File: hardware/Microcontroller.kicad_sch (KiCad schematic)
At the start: 93 parts, among them J10 UART, J2 USB_C, J3 OLED, J8 +12V, J9 STLink, Q4 IRLML2244, Q5 MMBT3904, SW1 Button Up, SW2 Button Down, SW3 Reset, SW4 Button Escape, SW5 Button Left, SW6 Button Enter, SW7 Button Right, SW8 Button Power, U10 STM32F405RGTx, U11 TPS7A2033, U2 TP6841S6, U3 USBLC6-2, Y1 8 MHz

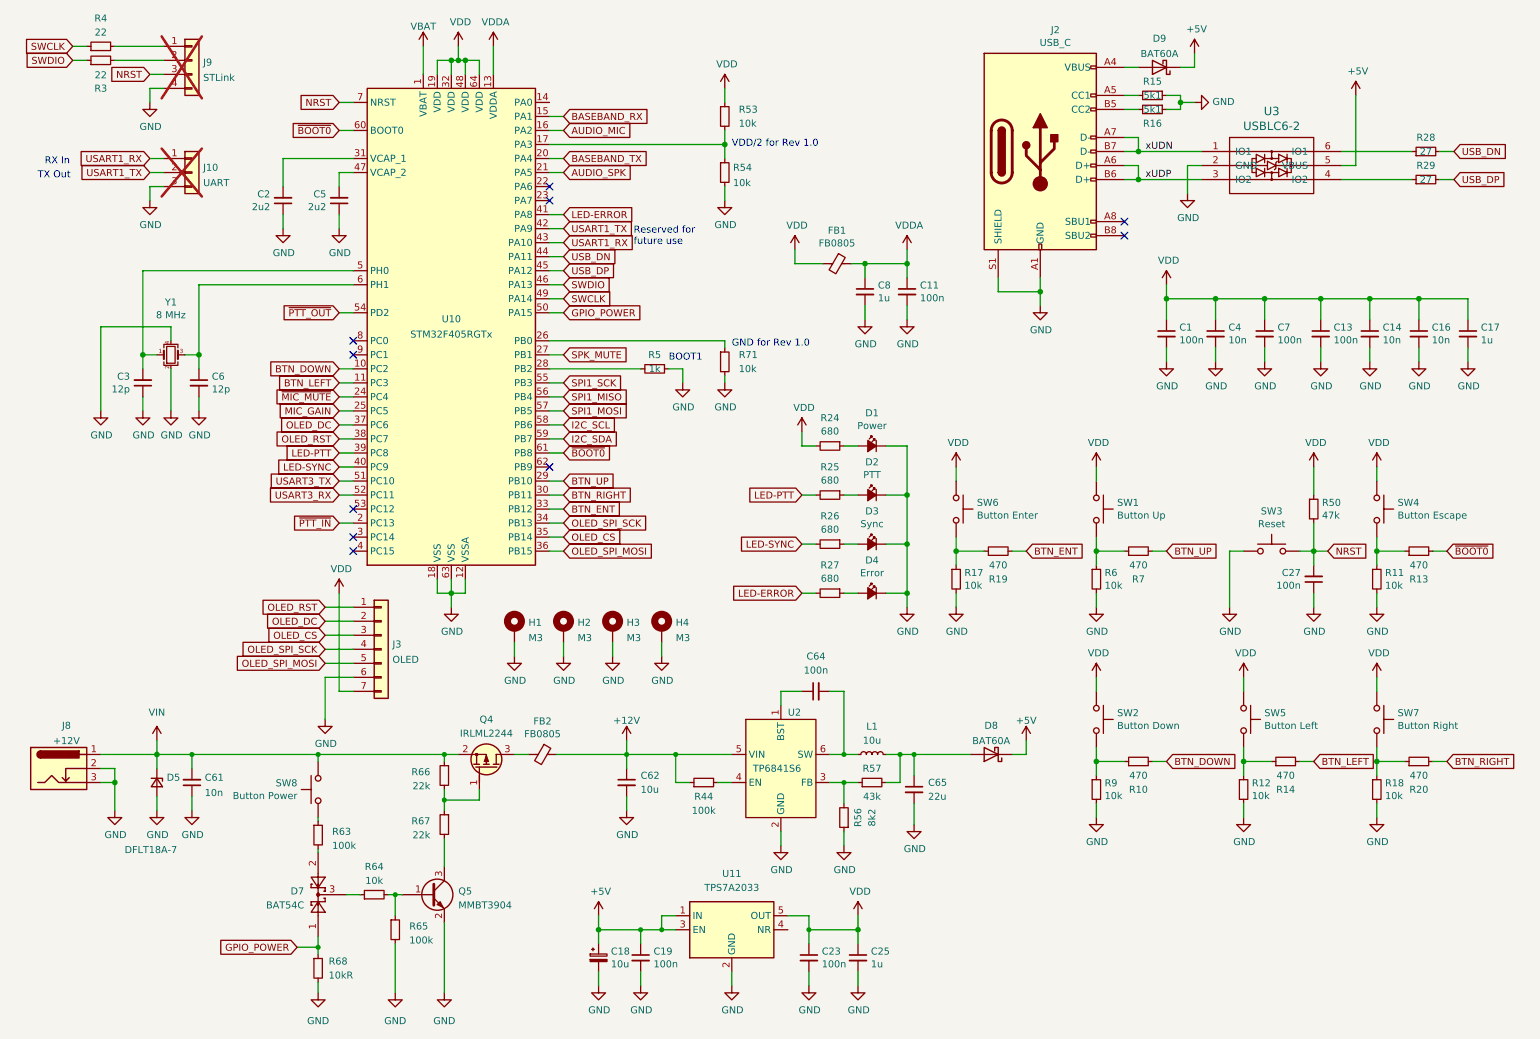
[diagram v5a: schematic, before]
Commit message: Reworked audio output diagram
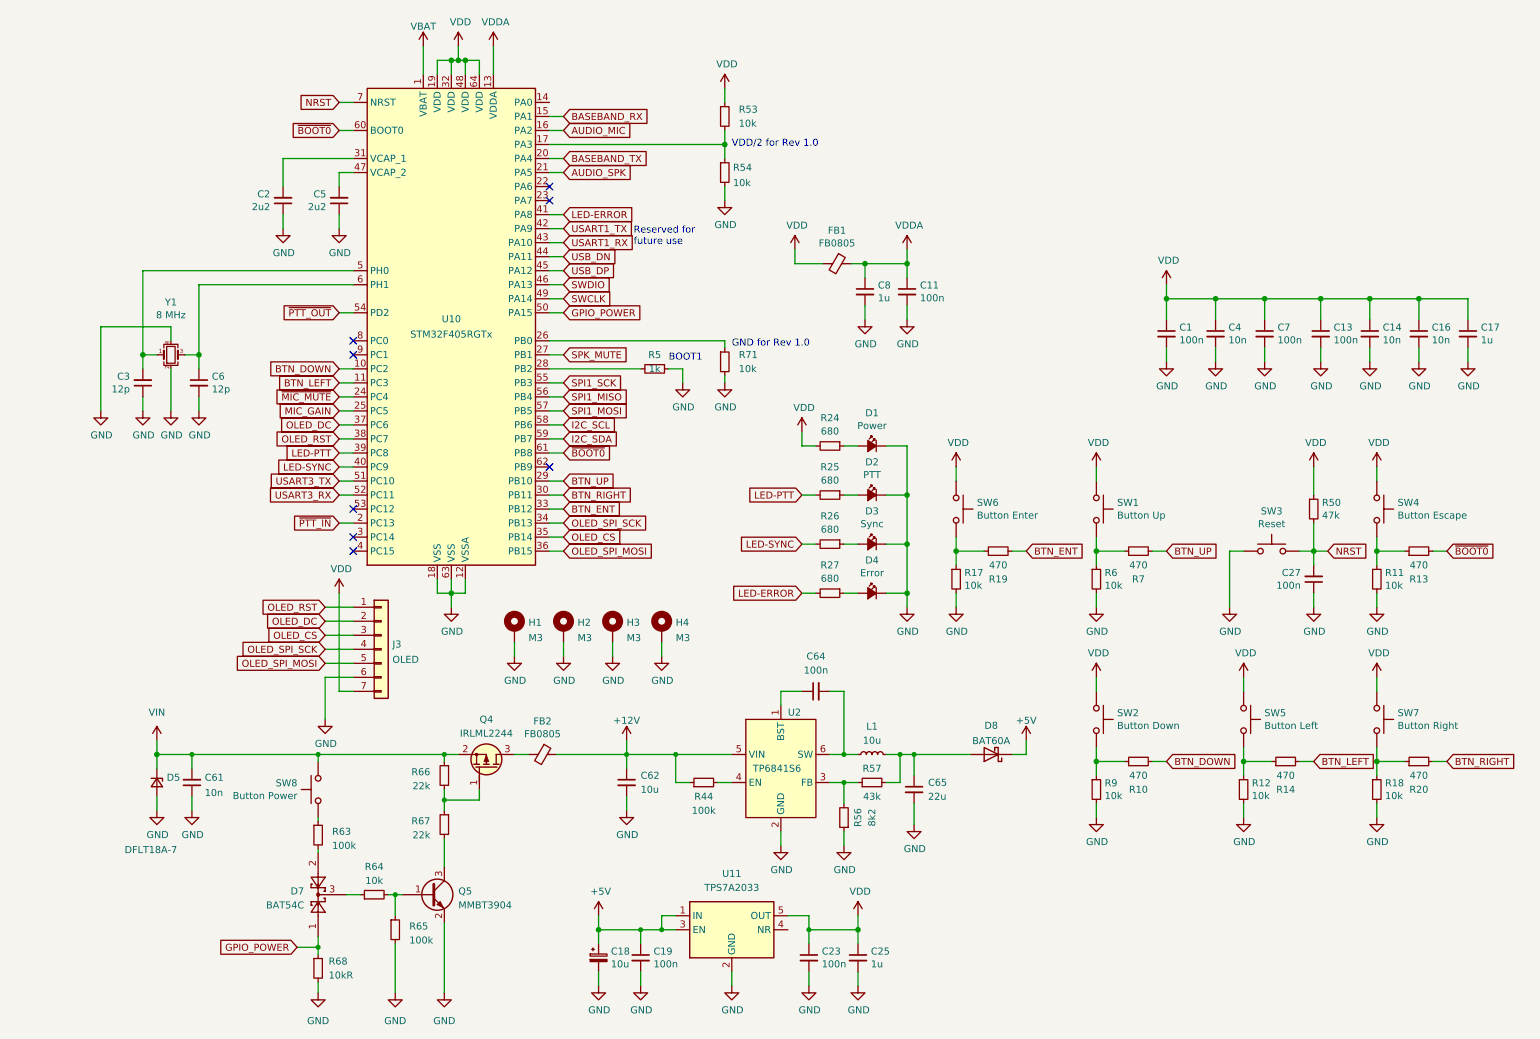
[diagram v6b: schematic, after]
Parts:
- removed D9: BAT60A, Diode_SMD:D_SOD-323, symbol Diode:BAT60A
- removed J10: UART, Connector_PinHeader_2.54mm:PinHeader_1x03_P2.54mm_Vertical, symbol Connector_Generic:Conn_01x03
- removed J2: USB_C, pkl_connectors:USB_C_Receptacle_HRO_TYPE-C-31-M-12, symbol Connector:USB_C_Receptacle_USB2.0
- removed J8: +12V, Connector_BarrelJack:BarrelJack_CLIFF_FC681465S_SMT_Horizontal, symbol Connector:Barrel_Jack_Switch_Pin3Ring
- removed J9: STLink, Connector_PinHeader_2.54mm:PinHeader_1x04_P2.54mm_Vertical, symbol Connector_Generic:Conn_01x04
- removed R15, R16: 5k1, pkl_dipol:R_0603, symbol pkl_device:pkl_R_Small
- removed R28, R29: 27, pkl_dipol:R_0603, symbol pkl_device:pkl_R_Small
- removed R3, R4: 22, pkl_dipol:R_0603, symbol pkl_device:pkl_R_Small
- removed U3: USBLC6-2, pkl_housings_sot:SOT-23-6, symbol pkl_misc:USBLC6-2
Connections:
- no-connect marks 10 -> 8
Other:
- note removed: "RX In"
- note removed: "TX Out"

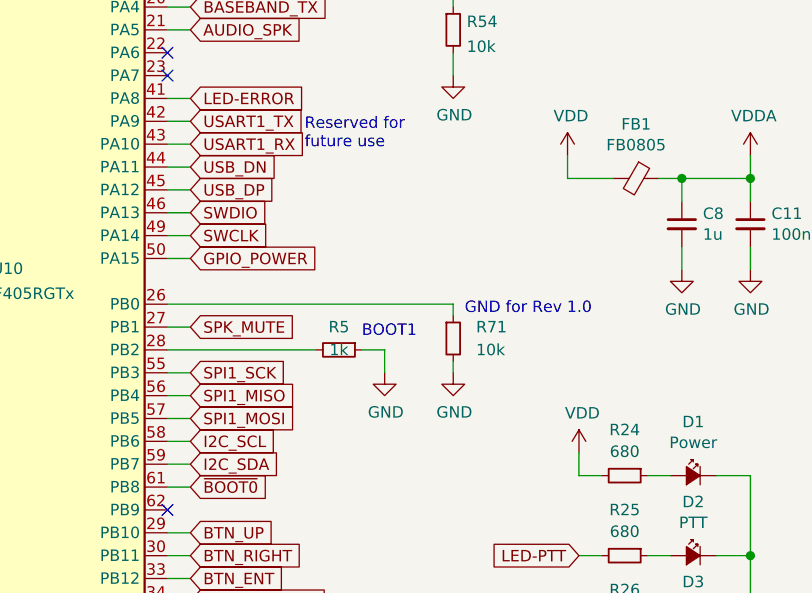
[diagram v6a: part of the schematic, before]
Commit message: [WIP] PCB layout and routing
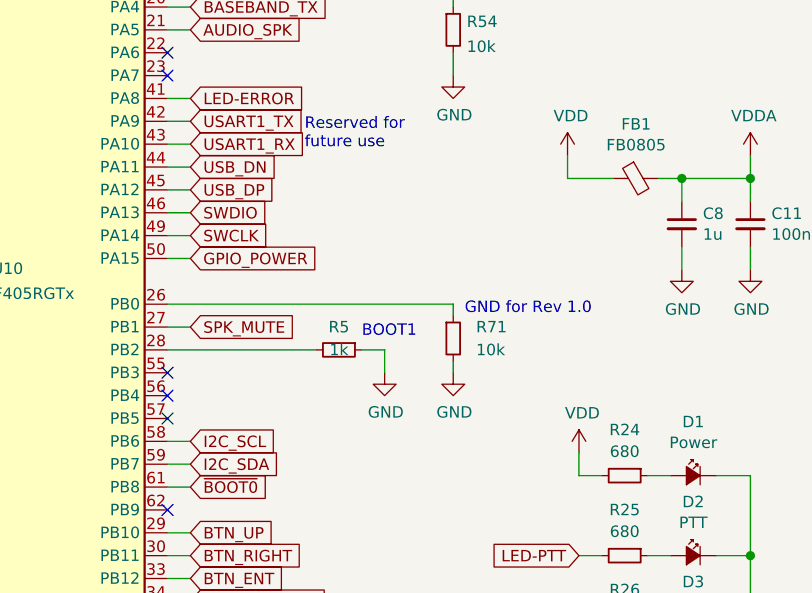
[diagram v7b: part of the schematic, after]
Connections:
- net VDD: now also FB1.1; no longer FB1.2
- net VDDA: now also FB1.2; no longer FB1.1
- net SPI1_MISO: no longer names the net of U10.56 (PB4)
- net SPI1_MOSI: no longer names the net of U10.57 (PB5)
- net SPI1_SCK: no longer names the net of U10.55 (PB3)
- no-connect marks 8 -> 11
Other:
- moved on the sheet: FB1
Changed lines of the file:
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@@
   (junction (at 165.1 179.07) (diameter 1.016) (color 0 0 0 0)
   )
+  (no_connect (at 109.22 82.55))
   (no_connect (at 109.22 95.25))
   (no_connect (at 109.22 44.45))
   (no_connect (at 73.66 110.49))
+  (no_connect (at 109.22 80.01))
   (no_connect (at 109.22 46.99))
   (no_connect (at 73.66 72.39))
   (no_connect (at 73.66 107.95))
   (no_connect (at 73.66 74.93))
+  (no_connect (at 109.22 85.09))
   (no_connect (at 73.66 102.87))
   (wire (pts (xy 91.44 115.57) (xy 91.44 118.11))
@@
     (stroke (width 0) (type solid))
   )
-  (wire (pts (xy 111.76 85.09) (xy 109.22 85.09))
-    (stroke (width 0) (type solid))
-  )
   (wire (pts (xy 140.97 72.39) (xy 140.97 73.66))
     (stroke (width 0) (type default))
@@
     (stroke (width 0) (type solid))
   )
-  (wire (pts (xy 111.76 82.55) (xy 109.22 82.55))
-    (stroke (width 0) (type solid))
-  )
   (wire (pts (xy 247.65 95.25) (xy 247.65 100.33))
     (stroke (width 0) (type default))
@@
   )
   (wire (pts (xy 71.12 105.41) (xy 73.66 105.41))
-    (stroke (width 0) (type solid))
-  )
-  (wire (pts (xy 109.22 80.01) (xy 111.76 80.01))
     (stroke (width 0) (type solid))
   )
@@
     )
   )
-  (global_label "SPI1_MOSI" (shape input) (at 111.76 85.09 0) (fields_autoplaced)
-    (effects (font (size 1.27 1.27)) (justify left))
-    (property "Intersheetrefs" "${INTERSHEET_REFS}" (at -8.89 -5.08 0)
-      (effects (font (size 1.27 1.27)) hide)
-    )
-  )
   (global_label "USB_DN" (shape input) (at 111.76 57.15 0) (fields_autoplaced)
     (effects (font (size 1.27 1.27)) (justify left))
@@
     )
   )
-  (global_label "SPI1_MISO" (shape input) (at 111.76 82.55 0) (fields_autoplaced)
-    (effects (font (size 1.27 1.27)) (justify left))
-    (property "Intersheetrefs" "${INTERSHEET_REFS}" (at -8.89 -5.08 0)
-      (effects (font (size 1.27 1.27)) hide)
-    )
-  )
   (global_label "NRST" (shape input) (at 250.19 110.49 0) (fields_autoplaced)
     (effects (font (size 1.27 1.27)) (justify left))
@@
     (effects (font (size 1.27 1.27)) (justify right))
     (property "Intersheetrefs" "${INTERSHEET_REFS}" (at 1.27 -17.78 0)
-      (effects (font (size 1.27 1.27)) hide)
-    )
-  )
-  (global_label "SPI1_SCK" (shape input) (at 111.76 80.01 0) (fields_autoplaced)
-    (effects (font (size 1.27 1.27)) (justify left))
-    (property "Intersheetrefs" "${INTERSHEET_REFS}" (at -8.89 -5.08 0)
       (effects (font (size 1.27 1.27)) hide)
     )
@@
     )
   )
-  (symbol (lib_id "Device:Ferrite_Bead_Small") (at 161.29 58.42 270) (unit 1)
+  (symbol (lib_id "Device:Ferrite_Bead_Small") (at 161.29 58.42 90) (mirror x) (unit 1)
     (in_bom yes) (on_board yes) (dnp no)
     (property "Reference" "FB1" (at 161.29 52.4002 90)

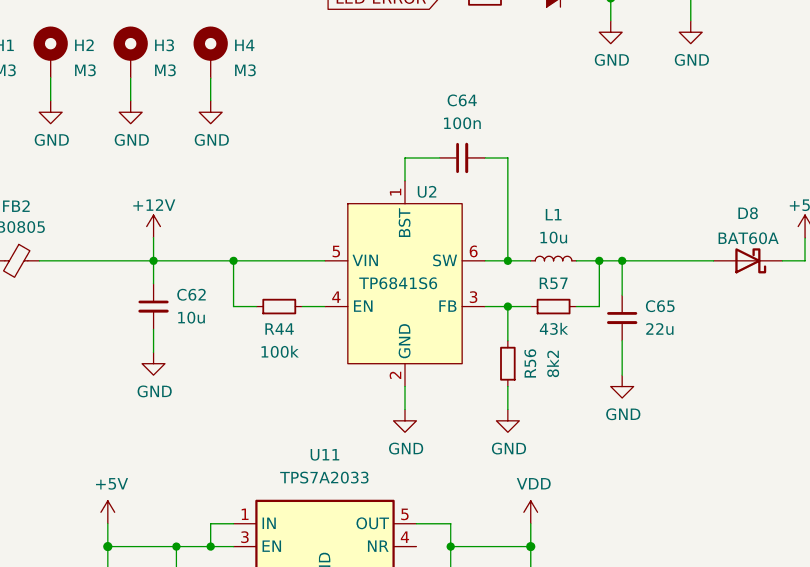
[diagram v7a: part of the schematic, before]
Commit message: Switched to M17_kicad_library for custom symbols/footprints
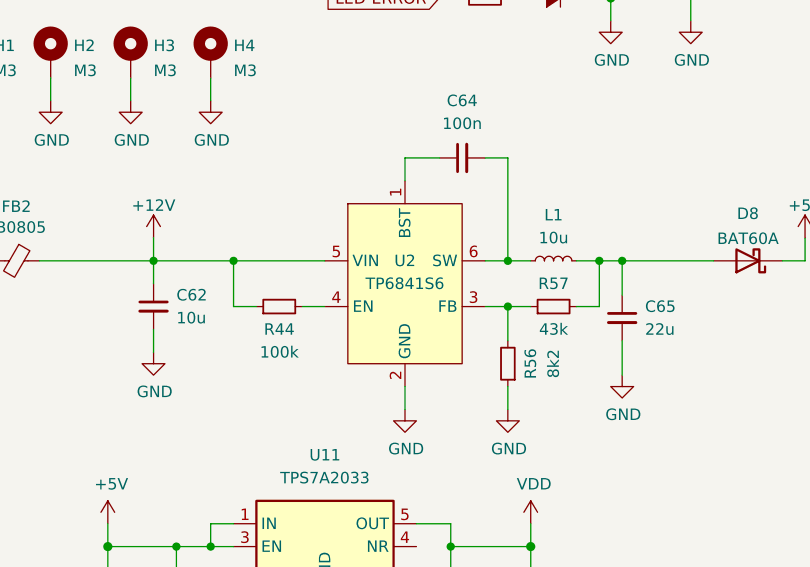
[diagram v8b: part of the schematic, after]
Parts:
- removed U2: TP6841S6, Package_TO_SOT_SMD:SOT-23-6, symbol Module17:TP6841S6
- added U2: TP6841S6, Package_TO_SOT_SMD:SOT-23-6, symbol M17_power:TP6841S6
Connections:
- net +12V: now also U2.5 (VIN)
- net GND: now also U2.2 (GND)
- net at R56.2, R57.1: now also U2.3 (FB)
- net at C64.2, L1.2: now also U2.6 (SW)
- net at C64.1: now also U2.1 (BST)
- net at R44.2: now also U2.4 (EN)
